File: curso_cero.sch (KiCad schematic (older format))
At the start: 24 parts, among them P1 Arduino Power header, P2 Arduino Analog header, P3 Analog pin, P4 Digital pin, P5 Servo 1, P6 Servo 2, P7 Arduino Digital H header, P8 Arduino Digital L header, P9 Power, SW1 SW_PUSH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

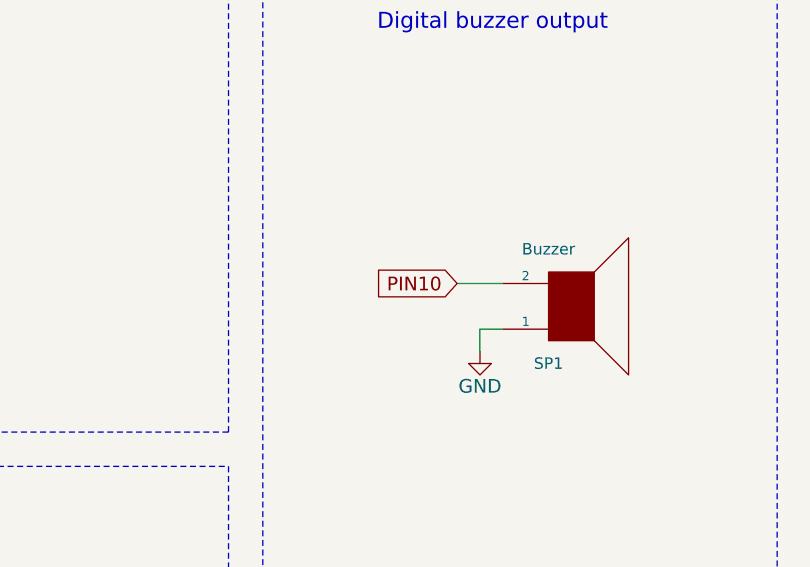
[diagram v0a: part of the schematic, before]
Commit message: corregido nombre de net pin D10
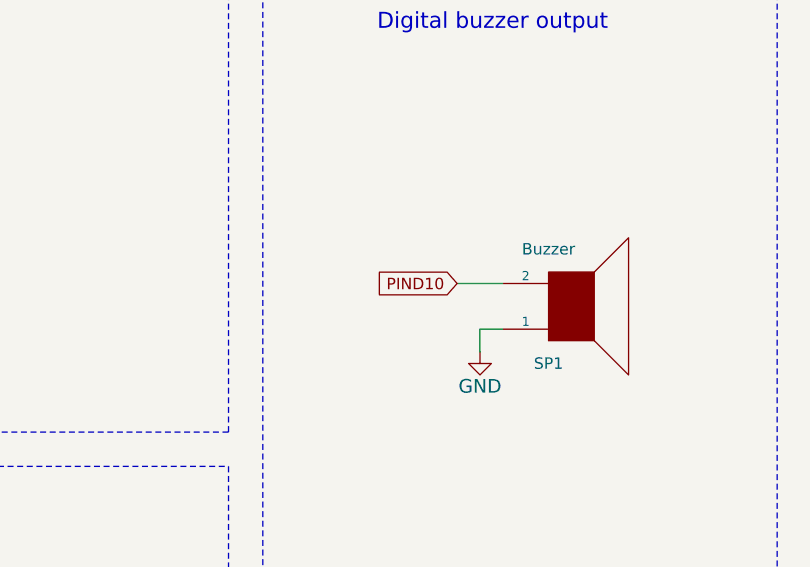
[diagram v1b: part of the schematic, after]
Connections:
- net PIN10 is gone; now on net PIND10: SP1.2
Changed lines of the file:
@@
 	1    0    0    -1
 $EndComp
-Text GLabel 6900 2000 0    60   Input ~ 0
-PIN10
+Text GLabel 6900 2000 0    50   Input ~ 0
+PIND10
 $Comp
 L SPEAKER SP1

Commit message: cambiado valores pulsadores
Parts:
- SW1, SW2: value SW_PUSH -> PULSA
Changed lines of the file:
@@
 P 4050 6150
 F 0 "SW1" V 3800 6250 50  0000 C CNN
-F 1 "SW_PUSH" H 4050 6070 50  0001 C CNN
+F 1 "PULSA" H 4050 6070 50  0001 C CNN
 F 2 "Buttons_Switches_ThroughHole:SW_PUSH_6mm_h5mm" H 4050 6150 60  0001 C CNN
 F 3 "" H 4050 6150 60  0000 C CNN
@@
 P 4850 6150
 F 0 "SW2" V 4600 6250 50  0000 C CNN
-F 1 "SW_PUSH" H 4850 6070 50  0001 C CNN
+F 1 "PULSA" H 4850 6070 50  0001 C CNN
 F 2 "Buttons_Switches_ThroughHole:SW_PUSH_6mm_h5mm" H 4850 6150 60  0001 C CNN
 F 3 "" H 4850 6150 60  0000 C CNN
